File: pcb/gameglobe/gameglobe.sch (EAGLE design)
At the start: 16 parts

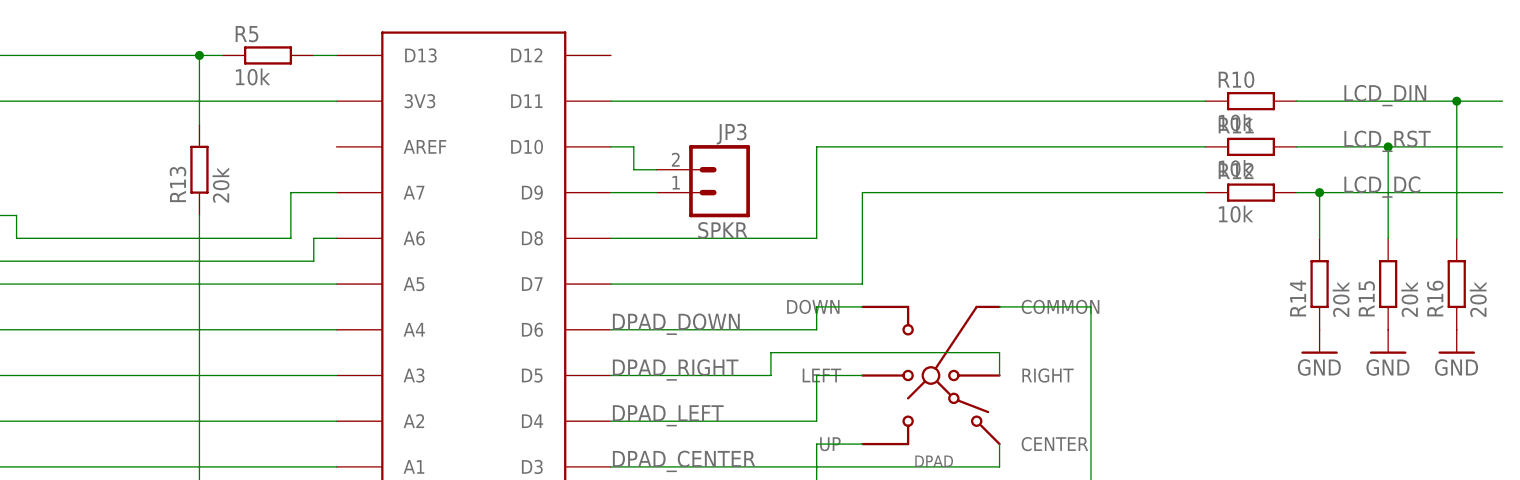
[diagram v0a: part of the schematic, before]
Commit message: Resistor renaming and related silkscreen fixes
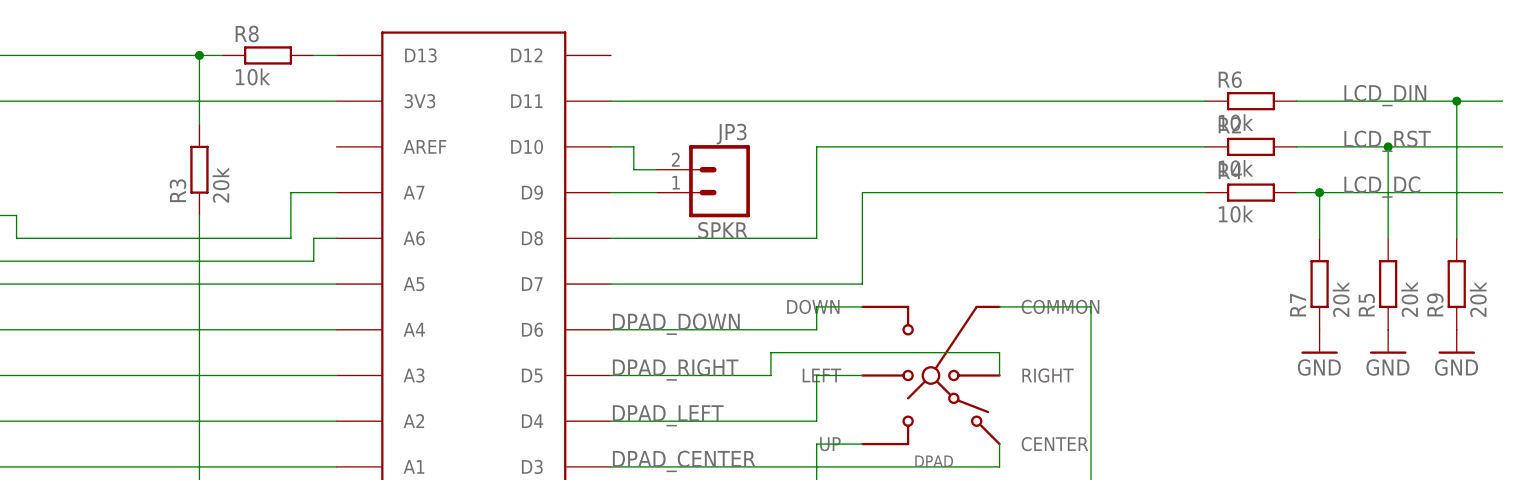
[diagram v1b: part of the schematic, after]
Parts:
- removed R15: 20k, resistor:R-EU_0411/15
- added R8: 10k, resistor:R-EU_0411/15
- R5: value 10k -> 20k
- renumbered R10 to R6, R11 to R2, R12 to R4, R13 to R3, R14 to R7, R16 to R9
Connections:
- net GND: now also R5.1; no longer R15.1
- net LCD_CLK: now also R8.1; no longer R5.1
- net LCD_RST: now also R5.2; no longer R15.2
- net N$1: now also R8.2; no longer R5.2
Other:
- moved on the sheet: R5
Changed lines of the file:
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@@
 </classes>
 <parts>
-<part name="R5" library="resistor" deviceset="R-EU_" device="0411/15" value="10k"/>
-<part name="R10" library="resistor" deviceset="R-EU_" device="0411/15" value="10k"/>
-<part name="R11" library="resistor" deviceset="R-EU_" device="0411/15" value="10k"/>
-<part name="R12" library="resistor" deviceset="R-EU_" device="0411/15" value="10k"/>
-<part name="R13" library="resistor" deviceset="R-EU_" device="0411/15" value="20k"/>
-<part name="R14" library="resistor" deviceset="R-EU_" device="0411/15" value="20k"/>
-<part name="R15" library="resistor" deviceset="R-EU_" device="0411/15" value="20k"/>
-<part name="R16" library="resistor" deviceset="R-EU_" device="0411/15" value="20k"/>
+<part name="R8" library="resistor" deviceset="R-EU_" device="0411/15" value="10k"/>
+<part name="R6" library="resistor" deviceset="R-EU_" device="0411/15" value="10k"/>
+<part name="R2" library="resistor" deviceset="R-EU_" device="0411/15" value="10k"/>
+<part name="R4" library="resistor" deviceset="R-EU_" device="0411/15" value="10k"/>
+<part name="R3" library="resistor" deviceset="R-EU_" device="0411/15" value="20k"/>
+<part name="R7" library="resistor" deviceset="R-EU_" device="0411/15" value="20k"/>
+<part name="R5" library="resistor" deviceset="R-EU_" device="0411/15" value="20k"/>
+<part name="R9" library="resistor" deviceset="R-EU_" device="0411/15" value="20k"/>
 <part name="GND1" library="supply1" deviceset="GND" device=""/>
 <part name="GND2" library="supply1" deviceset="GND" device=""/>
@@
 </plain>
 <instances>
-<instance part="R5" gate="G$1" x="93.98" y="96.52"/>
-<instance part="R10" gate="G$1" x="203.2" y="91.44"/>
-<instance part="R11" gate="G$1" x="203.2" y="86.36"/>
-<instance part="R12" gate="G$1" x="203.2" y="81.28"/>
-<instance part="R13" gate="G$1" x="86.36" y="83.82" rot="R90"/>
-<instance part="R14" gate="G$1" x="210.82" y="71.12" rot="R90"/>
-<instance part="R15" gate="G$1" x="218.44" y="71.12" rot="R90"/>
-<instance part="R16" gate="G$1" x="226.06" y="71.12" rot="R90"/>
+<instance part="R8" gate="G$1" x="93.98" y="96.52"/>
+<instance part="R6" gate="G$1" x="203.2" y="91.44"/>
+<instance part="R2" gate="G$1" x="203.2" y="86.36"/>
+<instance part="R4" gate="G$1" x="203.2" y="81.28"/>
+<instance part="R3" gate="G$1" x="86.36" y="83.82" rot="R90"/>
+<instance part="R7" gate="G$1" x="210.82" y="71.12" rot="R90"/>
+<instance part="R5" gate="G$1" x="218.44" y="71.12" rot="R90"/>
+<instance part="R9" gate="G$1" x="226.06" y="71.12" rot="R90"/>
 <instance part="GND1" gate="1" x="152.4" y="2.54"/>
 <instance part="GND2" gate="1" x="86.36" y="2.54"/>
@@
 </segment>
 <segment>
-<pinref part="R11" gate="G$1" pin="2"/>
+<pinref part="R2" gate="G$1" pin="2"/>
 <wire x1="208.28" y1="86.36" x2="218.44" y2="86.36" width="0.1524" layer="91"/>
 <wire x1="218.44" y1="86.36" x2="218.44" y2="76.2" width="0.1524" layer="91"/>
-<pinref part="R15" gate="G$1" pin="2"/>
+<pinref part="R5" gate="G$1" pin="2"/>
 <wire x1="218.44" y1="86.36" x2="231.14" y2="86.36" width="0.1524" layer="91"/>
 <junction x="218.44" y="86.36"/>
@@
 </segment>
 <segment>
-<pinref part="R12" gate="G$1" pin="2"/>
-<pinref part="R14" gate="G$1" pin="2"/>
+<pinref part="R4" gate="G$1" pin="2"/>
+<pinref part="R7" gate="G$1" pin="2"/>
 <wire x1="208.28" y1="81.28" x2="210.82" y2="81.28" width="0.1524" layer="91"/>
 <wire x1="210.82" y1="81.28" x2="210.82" y2="76.2" width="0.1524" layer="91"/>
@@
 </segment>
 <segment>
-<pinref part="R10" gate="G$1" pin="2"/>
+<pinref part="R6" gate="G$1" pin="2"/>
 <wire x1="208.28" y1="91.44" x2="226.06" y2="91.44" width="0.1524" layer="91"/>
 <wire x1="226.06" y1="91.44" x2="226.06" y2="76.2" width="0.1524" layer="91"/>
-<pinref part="R16" gate="G$1" pin="2"/>
+<pinref part="R9" gate="G$1" pin="2"/>
 <wire x1="226.06" y1="91.44" x2="231.14" y2="91.44" width="0.1524" layer="91"/>
 <junction x="226.06" y="91.44"/>
@@
 </segment>
 <segment>
-<pinref part="R13" gate="G$1" pin="2"/>
+<pinref part="R3" gate="G$1" pin="2"/>
 <wire x1="86.36" y1="88.9" x2="86.36" y2="96.52" width="0.1524" layer="91"/>
-<pinref part="R5" gate="G$1" pin="1"/>
+<pinref part="R8" gate="G$1" pin="1"/>
 <wire x1="86.36" y1="96.52" x2="88.9" y2="96.52" width="0.1524" layer="91"/>
 <wire x1="86.36" y1="96.52" x2="12.7" y2="96.52" width="0.1524" layer="91"/>
@@
 <net name="N$1" class="0">
 <segment>
-<pinref part="R5" gate="G$1" pin="2"/>
+<pinref part="R8" gate="G$1" pin="2"/>
 <wire x1="99.06" y1="96.52" x2="101.6" y2="96.52" width="0.1524" layer="91"/>
 <pinref part="ARDUINO_NANO" gate="G$1" pin="D13"/>
@@
 <segment>
 <wire x1="160.02" y1="71.12" x2="160.02" y2="81.28" width="0.1524" layer="91"/>
-<pinref part="R12" gate="G$1" pin="1"/>
+<pinref part="R4" gate="G$1" pin="1"/>
 <wire x1="160.02" y1="81.28" x2="198.12" y2="81.28" width="0.1524" layer="91"/>
 <pinref part="ARDUINO_NANO" gate="G$1" pin="D7"/>
@@
 <segment>
 <pinref part="ARDUINO_NANO" gate="G$1" pin="D11"/>
-<pinref part="R10" gate="G$1" pin="1"/>
+<pinref part="R6" gate="G$1" pin="1"/>
 <wire x1="132.08" y1="91.44" x2="198.12" y2="91.44" width="0.1524" layer="91"/>
 </segment>
@@
 <net name="N$3" class="0">
 <segment>
-<pinref part="R11" gate="G$1" pin="1"/>
+<pinref part="R2" gate="G$1" pin="1"/>
 <wire x1="198.12" y1="86.36" x2="154.94" y2="86.36" width="0.1524" layer="91"/>
 <wire x1="154.94" y1="86.36" x2="154.94" y2="76.2" width="0.1524" layer="91"/>
@@
 <wire x1="27.94" y1="30.48" x2="27.94" y2="48.26" width="0.1524" layer="91"/>
 <junction x="27.94" y="30.48"/>
-<pinref part="R13" gate="G$1" pin="1"/>
+<pinref part="R3" gate="G$1" pin="1"/>
 <wire x1="86.36" y1="78.74" x2="86.36" y2="30.48" width="0.1524" layer="91"/>
 <pinref part="BATTERY" gate="G$1" pin="-"/>
@@
 </segment>
 <segment>
-<pinref part="R14" gate="G$1" pin="1"/>
+<pinref part="R7" gate="G$1" pin="1"/>
 <pinref part="GND5" gate="1" pin="GND"/>
 </segment>
 <segment>
-<pinref part="R15" gate="G$1" pin="1"/>
+<pinref part="R5" gate="G$1" pin="1"/>
 <pinref part="GND6" gate="1" pin="GND"/>
 </segment>
 <segment>
-<pinref part="R16" gate="G$1" pin="1"/>
+<pinref part="R9" gate="G$1" pin="1"/>
 <pinref part="GND7" gate="1" pin="GND"/>
 </segment>

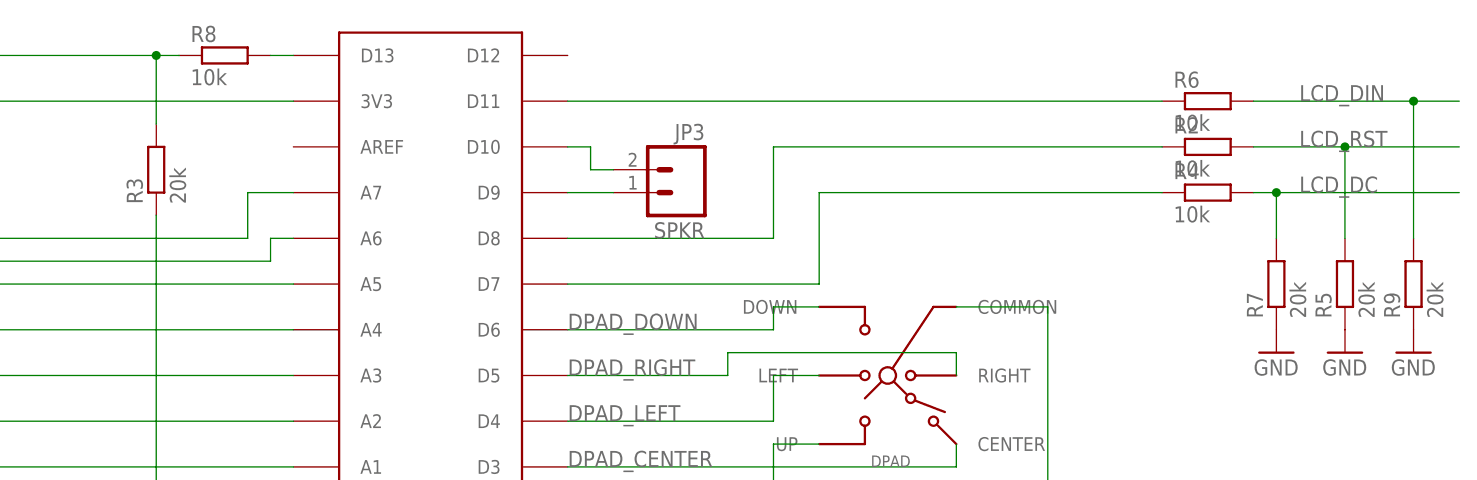
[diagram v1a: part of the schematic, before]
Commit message: New generic silkscreen design
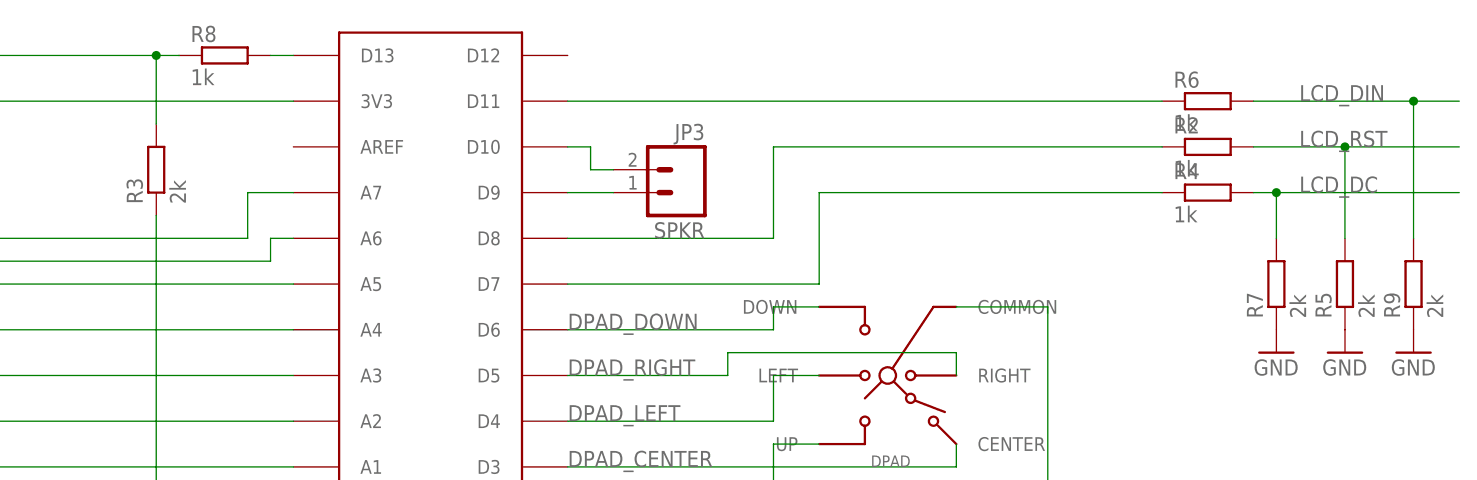
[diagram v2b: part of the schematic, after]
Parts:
- R2, R4, R6, R8: value 10k -> 1k
- R3, R5, R7, R9: value 20k -> 2k
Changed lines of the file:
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@@
 </classes>
 <parts>
-<part name="R8" library="resistor" deviceset="R-EU_" device="0411/15" value="10k"/>
-<part name="R6" library="resistor" deviceset="R-EU_" device="0411/15" value="10k"/>
-<part name="R2" library="resistor" deviceset="R-EU_" device="0411/15" value="10k"/>
-<part name="R4" library="resistor" deviceset="R-EU_" device="0411/15" value="10k"/>
-<part name="R3" library="resistor" deviceset="R-EU_" device="0411/15" value="20k"/>
-<part name="R7" library="resistor" deviceset="R-EU_" device="0411/15" value="20k"/>
-<part name="R5" library="resistor" deviceset="R-EU_" device="0411/15" value="20k"/>
-<part name="R9" library="resistor" deviceset="R-EU_" device="0411/15" value="20k"/>
+<part name="R8" library="resistor" deviceset="R-EU_" device="0411/15" value="1k"/>
+<part name="R6" library="resistor" deviceset="R-EU_" device="0411/15" value="1k"/>
+<part name="R2" library="resistor" deviceset="R-EU_" device="0411/15" value="1k"/>
+<part name="R4" library="resistor" deviceset="R-EU_" device="0411/15" value="1k"/>
+<part name="R3" library="resistor" deviceset="R-EU_" device="0411/15" value="2k"/>
+<part name="R7" library="resistor" deviceset="R-EU_" device="0411/15" value="2k"/>
+<part name="R5" library="resistor" deviceset="R-EU_" device="0411/15" value="2k"/>
+<part name="R9" library="resistor" deviceset="R-EU_" device="0411/15" value="2k"/>
 <part name="GND1" library="supply1" deviceset="GND" device=""/>
 <part name="GND2" library="supply1" deviceset="GND" device=""/>
